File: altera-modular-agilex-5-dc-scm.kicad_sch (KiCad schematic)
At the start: 0 parts

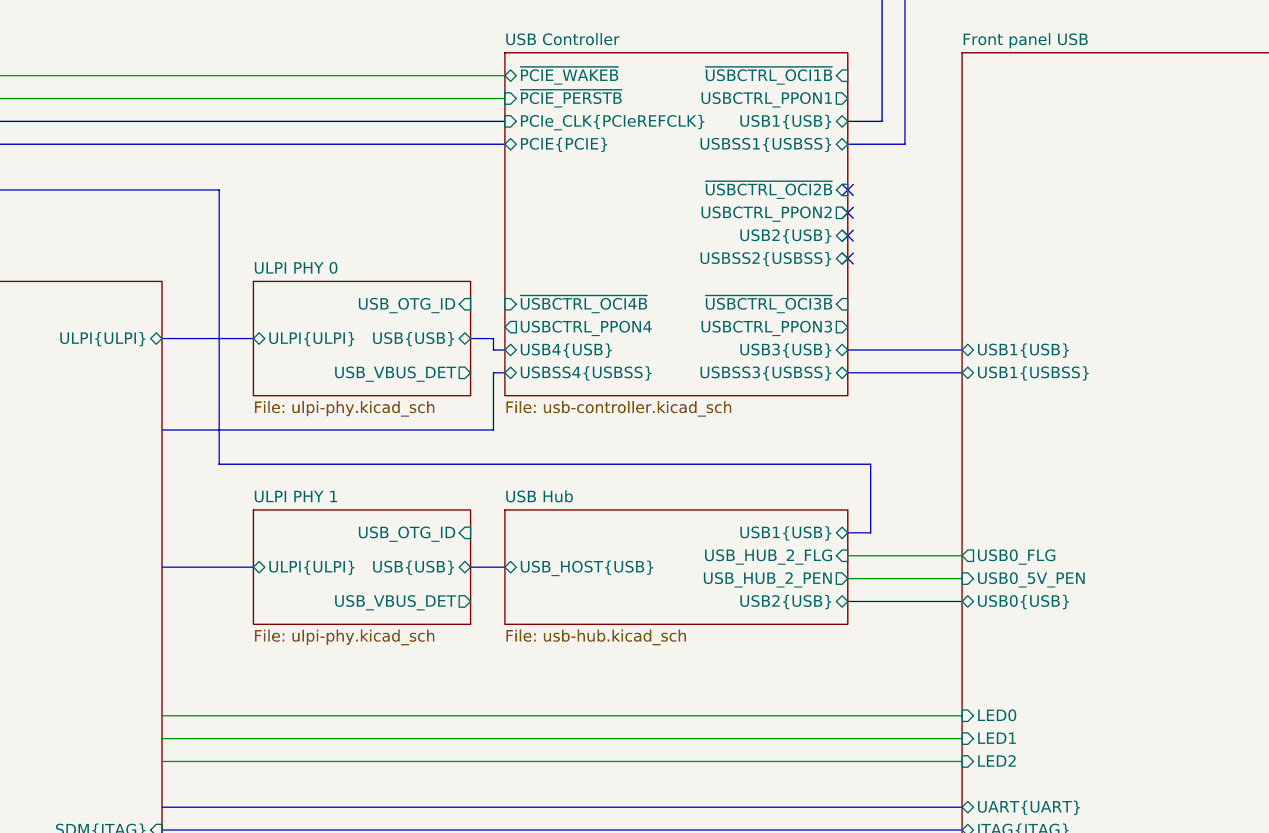
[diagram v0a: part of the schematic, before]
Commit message: [#99852] Connect USB ID, VBUS detect, PPONx and OCIxB signals
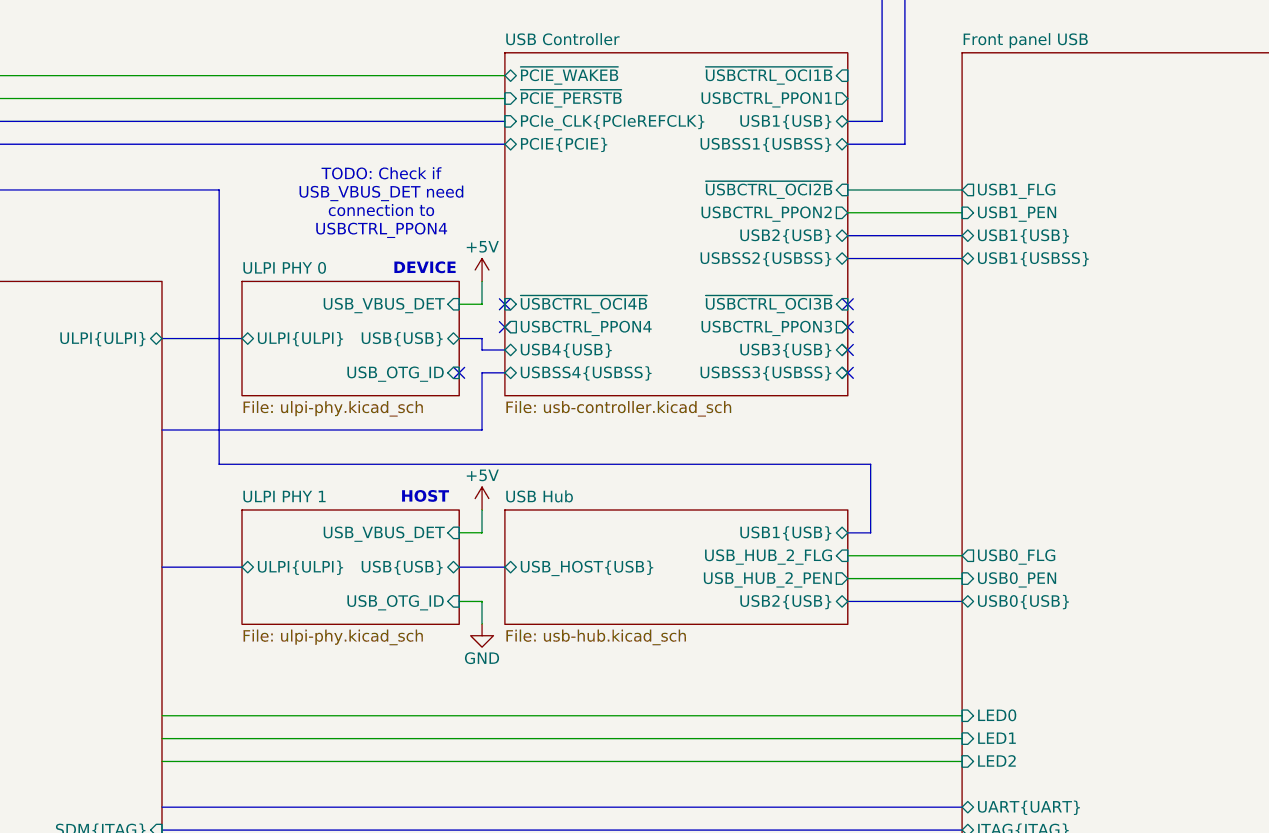
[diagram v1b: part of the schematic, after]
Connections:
- no-connect marks 4 -> 7
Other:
- sheet Front panel USB ports: added USB0_PEN, USB1_FLG, USB1_PEN; removed USB0_5V_PEN
- note added: "DEVICE"
- note added: "HOST"
- note added: "TODO: Check if USB_VBUS_DET need connection to USBCTRL_PPON4"

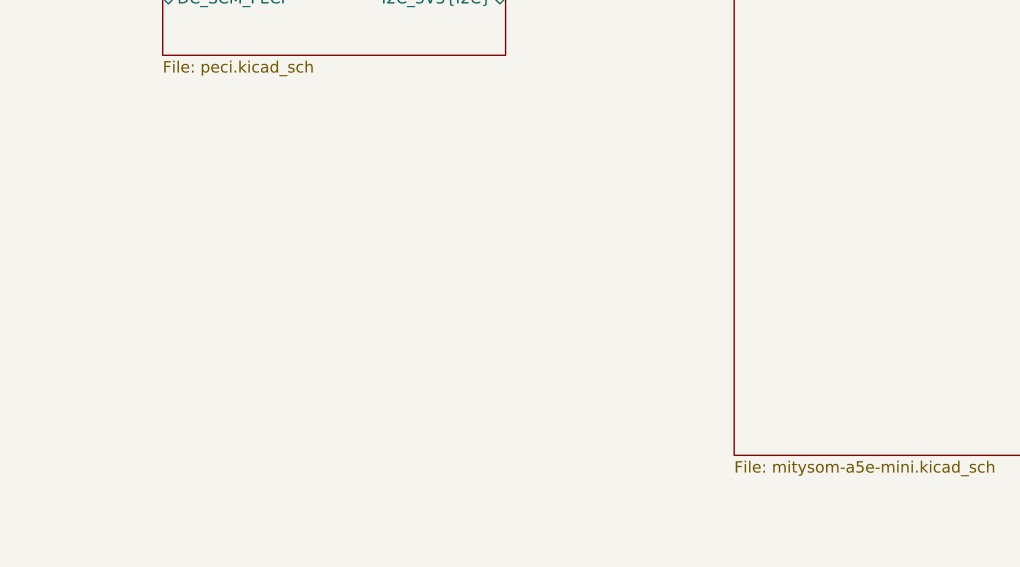
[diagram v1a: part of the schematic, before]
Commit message: [#99754] Add LTPI bias
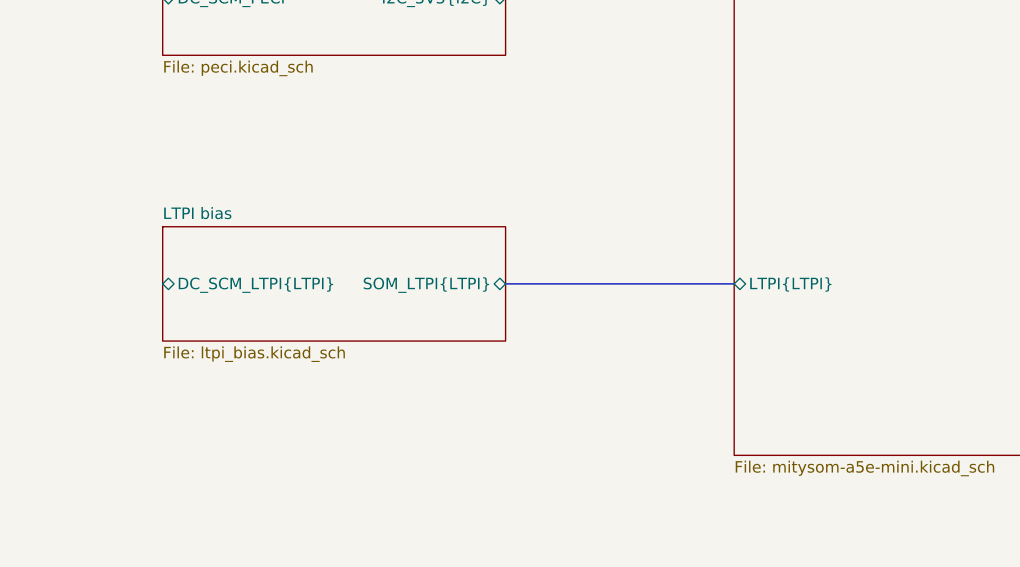
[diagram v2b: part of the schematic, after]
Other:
- added sheet LTPI bias (ltpi_bias.kicad_sch)
- sheet MitySOM-A5E Mini ports: added LTPI{LTPI}; removed none
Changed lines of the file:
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@@
+		)
+	)
+	(bus
+		(pts
+			(xy 139.7 158.75) (xy 165.1 158.75)
+		)
+		(stroke
+			(width 0)
+			(type default)
 		)
 	)
@@
 	)
 	(sheet
+		(at 101.6 152.4)
+		(size 38.1 12.7)
+		(exclude_from_sim no)
+		(in_bom yes)
+		(on_board yes)
+		(dnp no)
+		(fields_autoplaced yes)
+		(stroke
+			(width 0.1524)
+			(type solid)
+		)
+		(fill
+			(color 0 0 0 0)
+		)
+		(property "Sheetname" "LTPI bias"
+			(at 101.6 151.6884 0)
+			(show_name no)
+			(do_not_autoplace no)
+			(effects
+				(font
+					(size 1.27 1.27)
+				)
+				(justify left bottom)
+			)
+		)
+		(property "Sheetfile" "ltpi_bias.kicad_sch"
+			(at 101.6 165.6846 0)
+			(show_name no)
+			(do_not_autoplace no)
+			(effects
+				(font
+					(size 1.27 1.27)
+				)
+				(justify left top)
+			)
+		)
+		(pin "DC_SCM_LTPI{LTPI}" bidirectional
+			(at 101.6 158.75 180)
+			(effects
+				(font
+					(size 1.27 1.27)
+				)
+				(justify left)
+			)
+		)
+		(pin "SOM_LTPI{LTPI}" bidirectional
+			(at 139.7 158.75 0)
+			(effects
+				(font
+					(size 1.27 1.27)
+				)
+				(justify right)
+			)
+		)
+		(instances
+			(project "altera-modular-agilex-5-dc-scm"
+				(path "/6bb9d978-a328-4b30-874b-55170a976185"
+					(page "18")
+				)
+			)
+		)
+	)
+	(sheet
 		(at 165.1 63.5)
 		(size 101.6 114.3)
@@
 			)
 		)
+		(pin "LTPI{LTPI}" bidirectional
+			(at 165.1 158.75 180)
+			(effects
+				(font
+					(size 1.27 1.27)
+				)
+				(justify left)
+			)
+		)
